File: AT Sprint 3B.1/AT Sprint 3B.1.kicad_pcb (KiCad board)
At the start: 2 copper layers, 88.9 x 53.3 mm, 151 parts, among them J1 FilterBoard, J2 Jack-DC, J3 PADDLE IN, J4 IC-PROGRAMMING, J5 ANTENNA, J6 SPK, Q1 NDT2955, Q2 2N7002, Q3 2N7002, Q4 BS170, Q5 BS170, Q6 BS170, SW1 SW_Push, SW2 SW_Push, SW3 SW_Push, SW4 SW_Push, U1 SA612A, U10 812C35, U11 MCP120-3151, U2 SA612A, U22 KCSA02-107, U3 LM4808, U4 74LVC1G3157, U5 AN6123MS, U6 MSP430F1232IPW, U7 AD9834, U8 AC02, U9 812C50, X1 60Mhz, Y1 4.9152MHz, Y2 4.9152MHz, Y3 4.9152MHz, Y4 4.9152MHz, Y5 4.9152MHz, Y6 32.768k

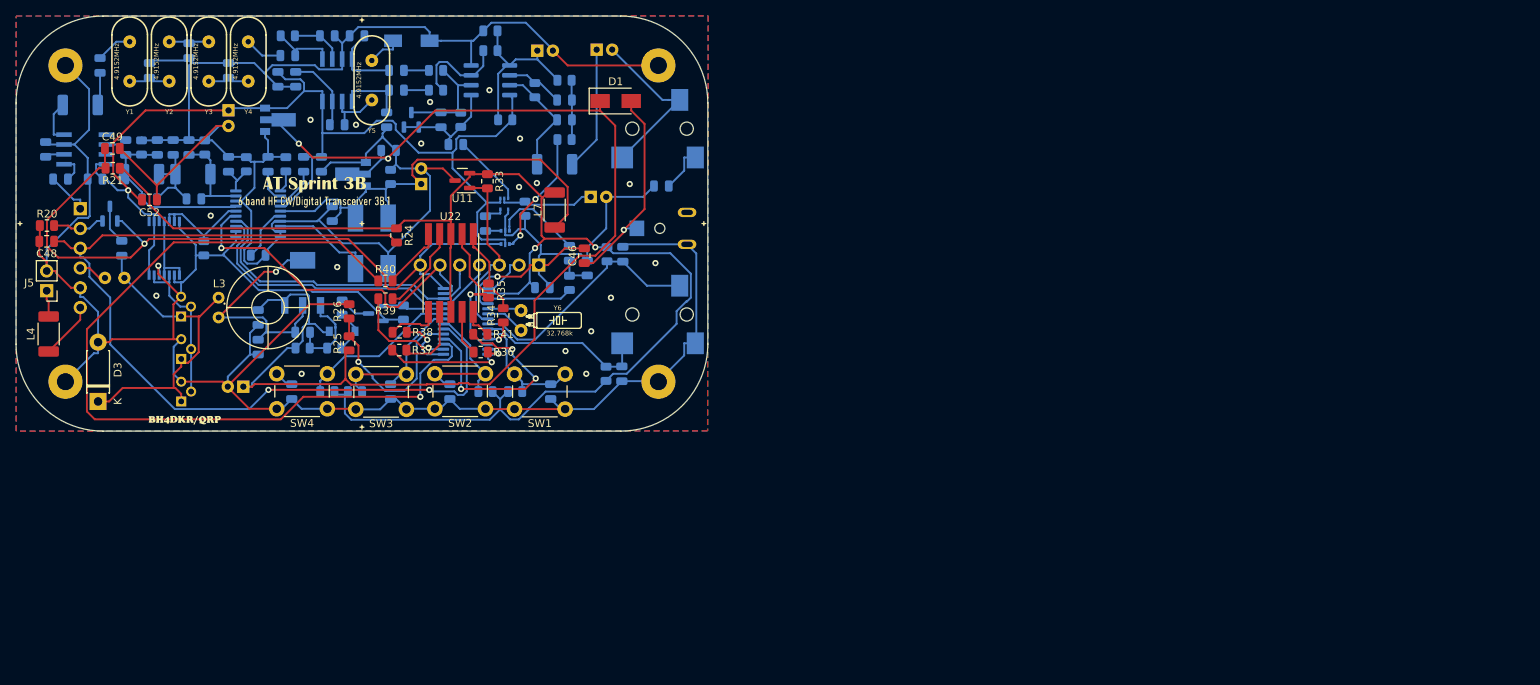
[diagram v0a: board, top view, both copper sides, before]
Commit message: add filter boundary in User.Drawing layer, fit room for filter board
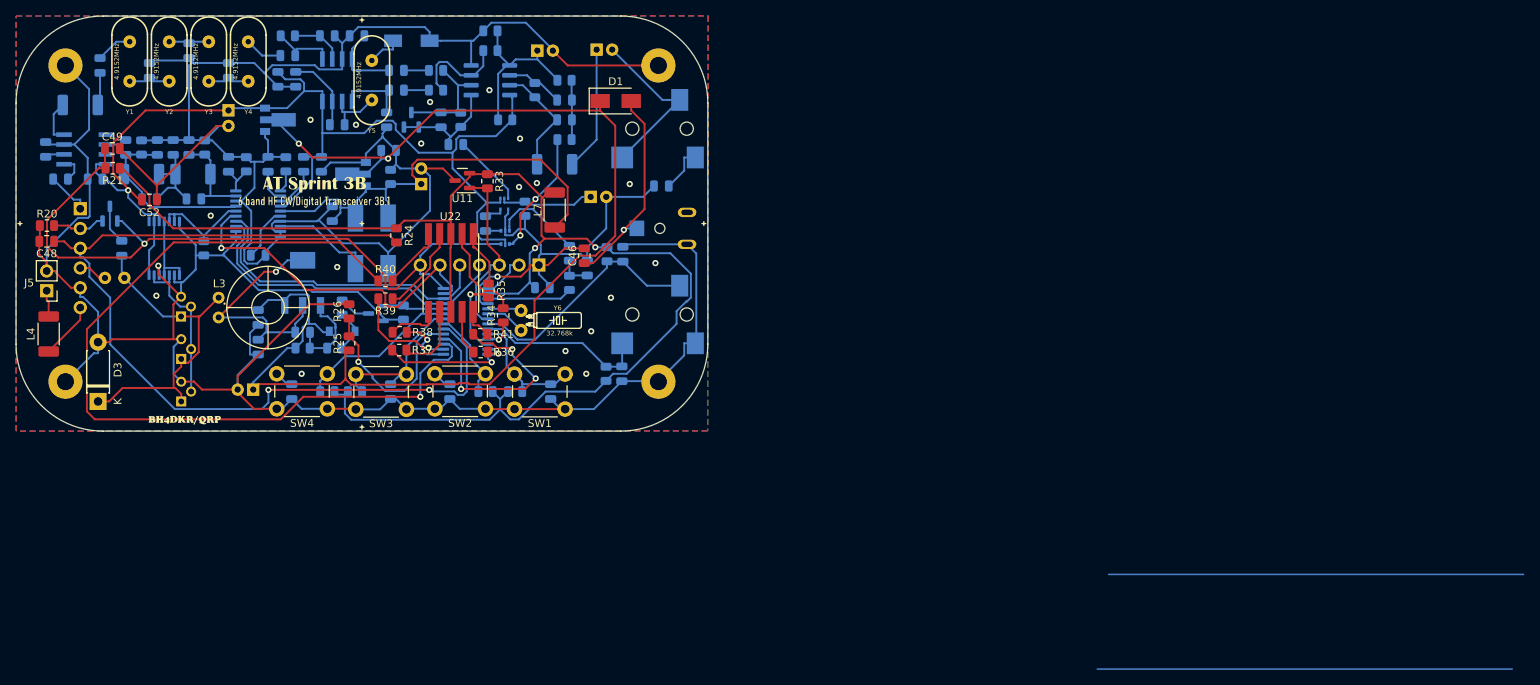
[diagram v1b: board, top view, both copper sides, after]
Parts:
- moved C56 1.33 mm to (64.1, 120.4)
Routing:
- net V+: track 161.8 -> 160.3 mm
- net /ATS3B1-MCU-DDS-TX/BAND_V: track 120.0 -> 121.0 mm
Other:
- board text added: "RF"

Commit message: fix C11 footprint
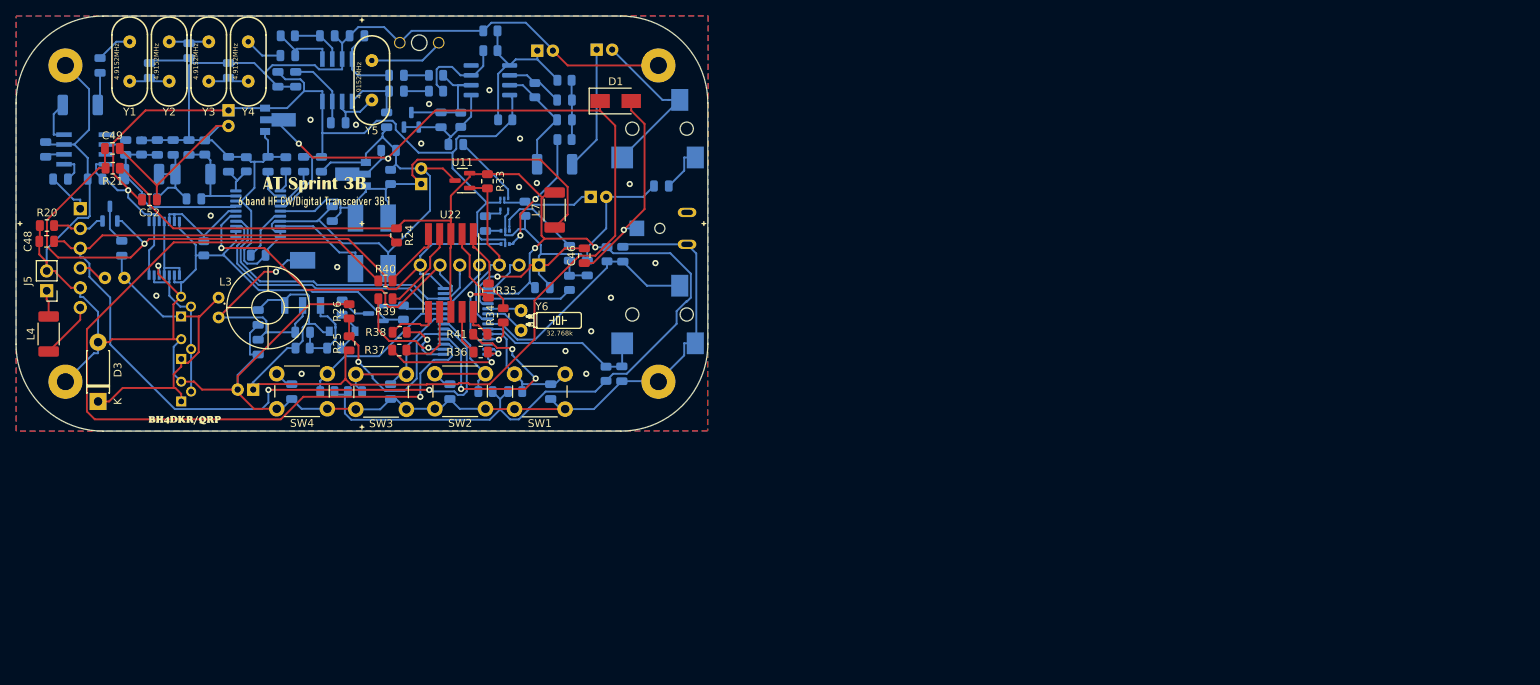
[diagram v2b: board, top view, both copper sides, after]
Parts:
- CT1: footprint Capacitor_SMD:C_Trimmer_Murata_TZB4-A -> CraftsmanICs:C_TRIMMER_TZ03
- moved CT1 1.05 mm to (85.5, 75.8)
- moved C15 0.64 mm to (82.5, 80.0)
- moved R2 0.64 mm to (87.6, 80.0)
- moved C11 0.28 mm to (75.1, 86.1)
- moved C16 0.13 mm to (82.5, 82.0)
- moved R4 0.13 mm to (87.6, 82.0)
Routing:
- net Net-(CT1-Pad1): track 4.44 -> 9.46 mm
- net GNDREF: track 557.0 -> 553.3 mm
- net Net-(C17-Pad2): track 14.3 -> 15.7 mm
- net Net-(R3-Pad2): track 13.0 -> 12.2 mm
- net Net-(C13-Pad1): track 8.88 -> 8.19 mm

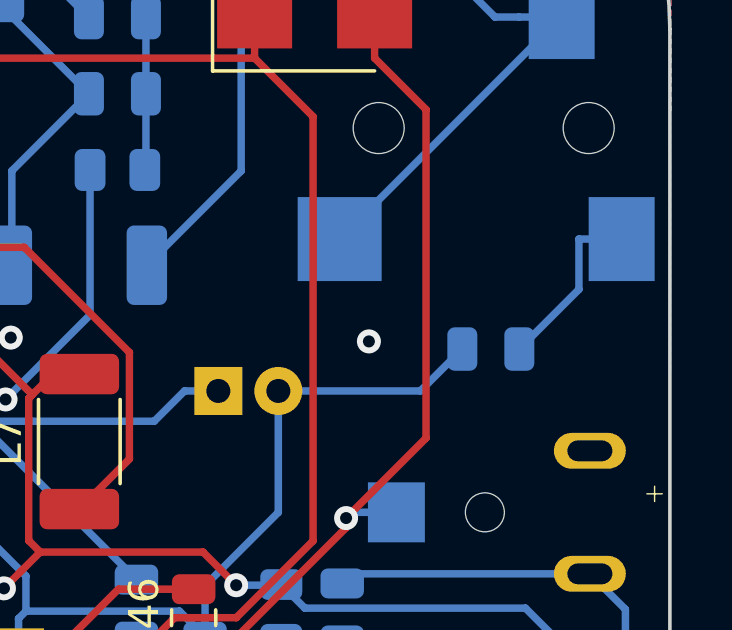
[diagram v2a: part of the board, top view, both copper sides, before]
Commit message: fix C22 TRS connection error
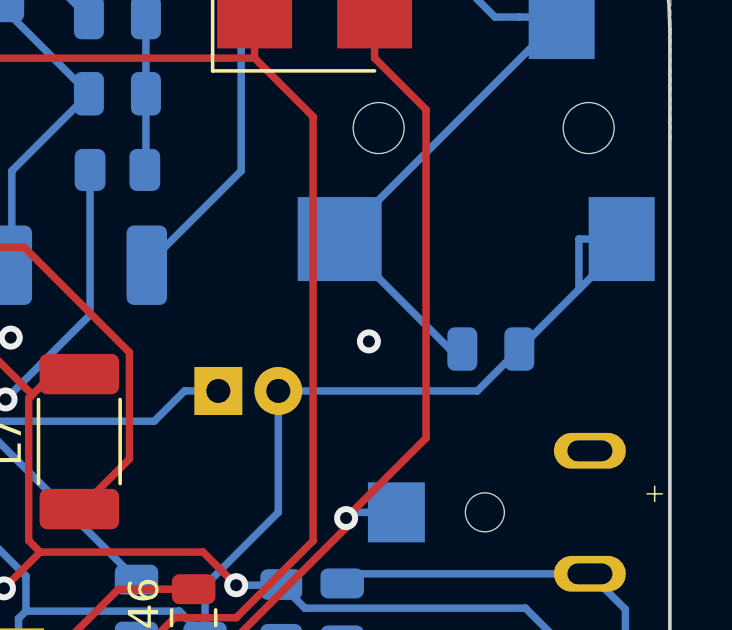
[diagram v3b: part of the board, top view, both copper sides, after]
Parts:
- turned C22 to 0 degrees
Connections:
- C22 pad 1: Net-(C22-Pad1) -> Net-(C54-Pad2)
- J6 pad S: Net-(C22-Pad1) -> GNDREF
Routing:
- net GNDREF: track 553.3 -> 563.4 mm
- net Net-(C22-Pad1): track 5.91 -> 0.00 mm
- net Net-(C54-Pad2): track 21.8 -> 27.4 mm

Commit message: fix some errors. release for pcb production
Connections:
- C49 pad 1: MUTE -> Net-(C49-Pad1)
- Q2 pad 1: MUTE -> Net-(C49-Pad1)
- R21 pad 1: MUTE -> Net-(C49-Pad1)
- R21 pad 2: VCC -> MUTE
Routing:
- net VCC: track 182.7 -> 143.2 mm
- net MUTE: track 92.3 -> 70.7 mm, vias 1 -> 2
- net Net-(C49-Pad1): track 0.00 -> 10.0 mm, vias 0 -> 1
